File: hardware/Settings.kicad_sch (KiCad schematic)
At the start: 10 parts

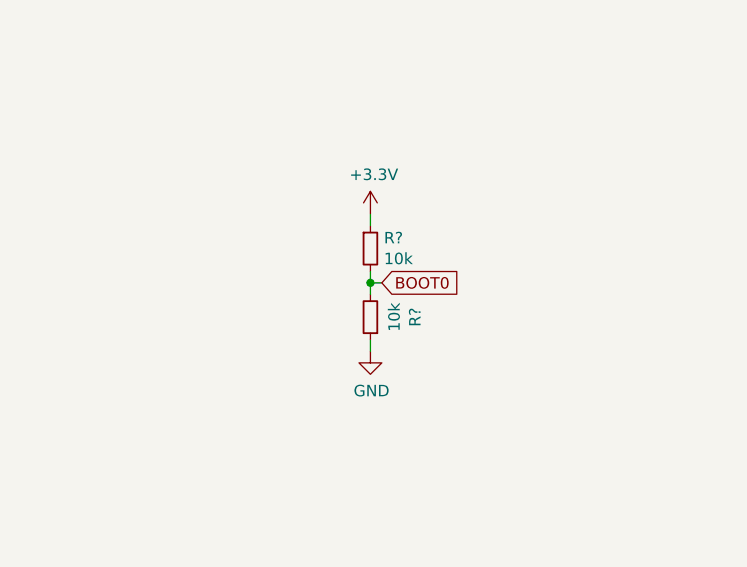
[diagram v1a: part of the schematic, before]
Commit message: added additional USB port and overall board update
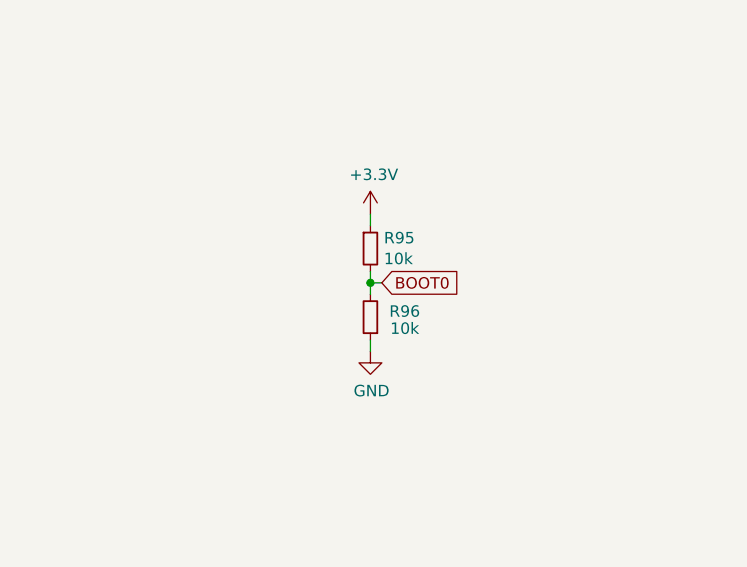
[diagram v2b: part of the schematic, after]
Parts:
- gave numbers to parts that had none: 2
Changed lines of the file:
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@@
   (symbol (lib_id "power:GND") (at 116.84 114.3 0) (unit 1)
     (in_bom yes) (on_board yes)
-    (property "Reference" "#PWR?" (id 0) (at 116.84 120.65 0)
+    (property "Reference" "#PWR0151" (id 0) (at 116.84 120.65 0)
       (effects (font (size 1.27 1.27)) hide)
     )
@@
   (symbol (lib_id "power:+3.3V") (at 227.965 85.09 0) (unit 1)
     (in_bom yes) (on_board yes)
-    (property "Reference" "#PWR?" (id 0) (at 227.965 88.9 0)
+    (property "Reference" "#PWR0153" (id 0) (at 227.965 88.9 0)
       (effects (font (size 1.27 1.27)) hide)
     )
@@
   (symbol (lib_id "power:GND") (at 93.345 114.3 0) (unit 1)
     (in_bom yes) (on_board yes)
-    (property "Reference" "#PWR?" (id 0) (at 93.345 120.65 0)
+    (property "Reference" "#PWR0149" (id 0) (at 93.345 120.65 0)
       (effects (font (size 1.27 1.27)) hide)
     )
@@
   (symbol (lib_id "Device:R_Small") (at 227.965 88.9 0) (unit 1)
     (in_bom yes) (on_board yes)
-    (property "Reference" "R?" (id 0) (at 229.4636 87.7316 0)
+    (property "Reference" "R95" (id 0) (at 229.4636 87.7316 0)
       (effects (font (size 1.27 1.27)) (justify left))
     )
@@
   (symbol (lib_id "power:GND") (at 74.93 114.3 0) (unit 1)
     (in_bom yes) (on_board yes)
-    (property "Reference" "#PWR?" (id 0) (at 74.93 120.65 0)
+    (property "Reference" "#PWR0150" (id 0) (at 74.93 120.65 0)
       (effects (font (size 1.27 1.27)) hide)
     )
@@
   (symbol (lib_id "power:GND") (at 227.965 100.33 0) (unit 1)
     (in_bom yes) (on_board yes)
-    (property "Reference" "#PWR?" (id 0) (at 227.965 106.68 0)
+    (property "Reference" "#PWR0152" (id 0) (at 227.965 106.68 0)
       (effects (font (size 1.27 1.27)) hide)
     )
@@
   (symbol (lib_id "Device:R_Small") (at 227.965 96.52 180) (unit 1)
     (in_bom yes) (on_board yes)
-    (property "Reference" "R?" (id 0) (at 232.9434 96.52 90))
-    (property "Value" "10k" (id 1) (at 230.632 96.52 90))
+    (property "Reference" "R96" (id 0) (at 231.775 95.885 0))
+    (property "Value" "10k" (id 1) (at 231.775 97.79 0))
     (property "Footprint" "Resistor_SMD:R_0603_1608Metric" (id 2) (at 227.965 96.52 0)
       (effects (font (size 1.27 1.27)) hide)
@@
   (symbol (lib_id "power:+3.3V") (at 93.345 99.06 0) (unit 1)
     (in_bom yes) (on_board yes)
-    (property "Reference" "#PWR?" (id 0) (at 93.345 102.87 0)
+    (property "Reference" "#PWR0147" (id 0) (at 93.345 102.87 0)
       (effects (font (size 1.27 1.27)) hide)
     )
@@
   (symbol (lib_id "power:+3.3V") (at 116.84 99.06 0) (unit 1)
     (in_bom yes) (on_board yes)
-    (property "Reference" "#PWR?" (id 0) (at 116.84 102.87 0)
+    (property "Reference" "#PWR0146" (id 0) (at 116.84 102.87 0)
       (effects (font (size 1.27 1.27)) hide)
     )
@@
   (symbol (lib_id "power:+3.3V") (at 74.93 99.06 0) (unit 1)
     (in_bom yes) (on_board yes)
-    (property "Reference" "#PWR?" (id 0) (at 74.93 102.87 0)
-      (effects (font (size 1.27 1.27)) hide)
-    )
+    (property "Reference" "#PWR0148" (id 0) (at 74.93 102.87 0)
+      (effects (font (size 1.27 1.27)) hide)
+    )

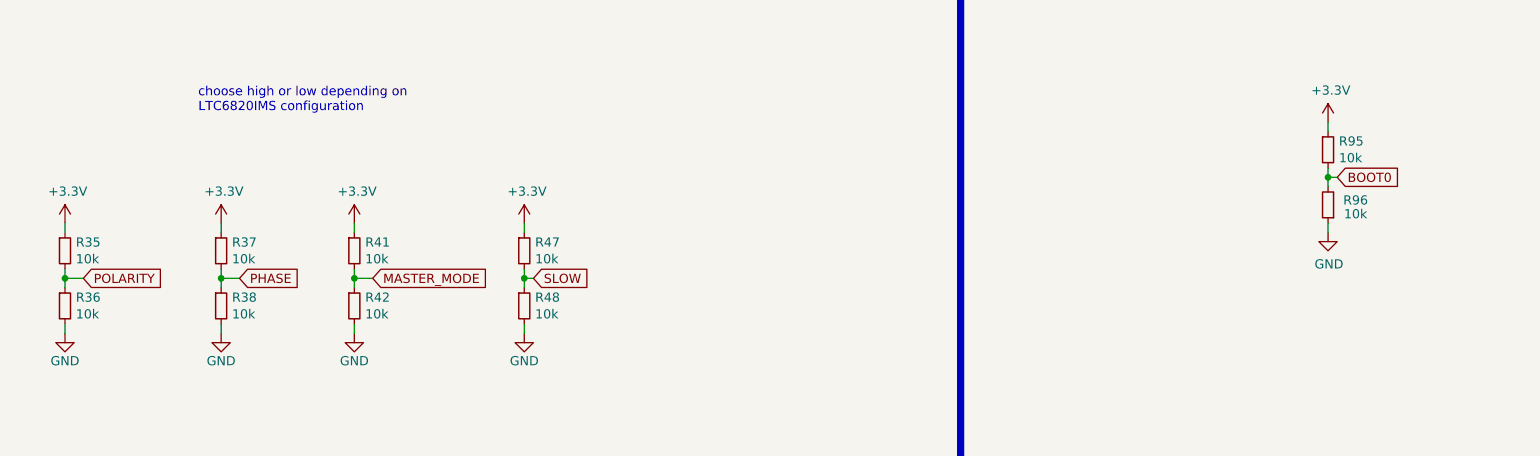
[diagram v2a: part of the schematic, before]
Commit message: Schematic readability update
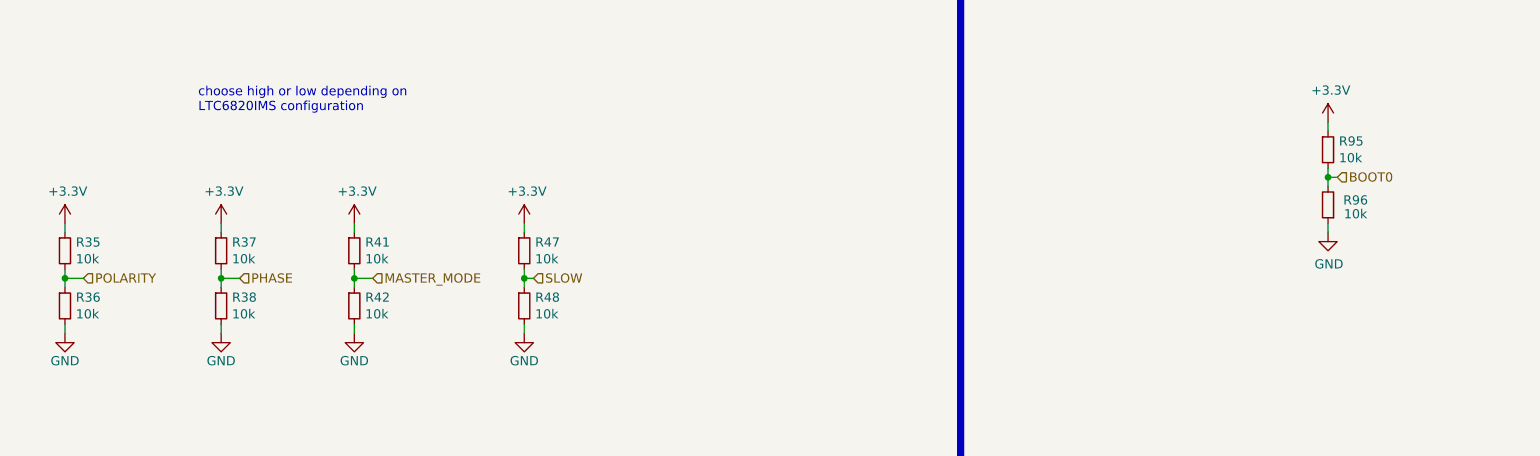
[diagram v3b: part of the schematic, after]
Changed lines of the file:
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@@
     (effects (font (size 5 5) (thickness 1) bold) (justify left bottom))
   )
-  (global_label "BOOT0" (shape input) (at 229.235 92.71 0) (fields_autoplaced)
+  (hierarchical_label "BOOT0" (shape input) (at 229.235 92.71 0)
     (effects (font (size 1.27 1.27)) (justify left))
-    (property "Intersheet References" "${INTERSHEET_REFS}" (id 0) (at 237.6673 92.7894 0)
-      (effects (font (size 1.27 1.27)) (justify left) hide)
-    )
   )
-  (global_label "POLARITY" (shape input) (at 55.88 106.68 0) (fields_autoplaced)
+  (hierarchical_label "POLARITY" (shape input) (at 55.88 106.68 0)
     (effects (font (size 1.27 1.27)) (justify left))
-    (property "Intersheet References" "${INTERSHEET_REFS}" (id 0) (at 66.8523 106.7594 0)
-      (effects (font (size 1.27 1.27)) (justify left) hide)
-    )
   )
-  (global_label "PHASE" (shape input) (at 77.47 106.68 0) (fields_autoplaced)
+  (hierarchical_label "SLOW" (shape input) (at 118.11 106.68 0)
     (effects (font (size 1.27 1.27)) (justify left))
-    (property "Intersheet References" "${INTERSHEET_REFS}" (id 0) (at 85.8418 106.6006 0)
-      (effects (font (size 1.27 1.27)) (justify left) hide)
-    )
   )
-  (global_label "SLOW" (shape input) (at 118.11 106.68 0) (fields_autoplaced)
+  (hierarchical_label "PHASE" (shape input) (at 77.47 106.68 0)
     (effects (font (size 1.27 1.27)) (justify left))
-    (property "Intersheet References" "${INTERSHEET_REFS}" (id 0) (at 125.4537 106.6006 0)
-      (effects (font (size 1.27 1.27)) (justify left) hide)
-    )
   )
-  (global_label "MASTER_MODE" (shape input) (at 95.885 106.68 0) (fields_autoplaced)
+  (hierarchical_label "MASTER_MODE" (shape input) (at 95.885 106.68 0)
     (effects (font (size 1.27 1.27)) (justify left))
-    (property "Intersheet References" "${INTERSHEET_REFS}" (id 0) (at 111.514 106.6006 0)
-      (effects (font (size 1.27 1.27)) (justify left) hide)
-    )
   )
   (symbol (lib_id "Device:R_Small") (at 74.93 102.87 0) (unit 1)

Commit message: remake in progress
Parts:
- removed R35, R36, R37, R38, R41, R42, R47, R48, R95, R96: 10k, Resistor_SMD:R_0603_1608Metric, symbol Device:R_Small
- added JP1: Polarity, Jumper:SolderJumper-3_P2.0mm_Open_TrianglePad1.0x1.5mm_NumberLabels, symbol Jumper:SolderJumper_3_Open
- added JP2, JP3: Phase, Jumper:SolderJumper-3_P2.0mm_Open_TrianglePad1.0x1.5mm_NumberLabels, symbol Jumper:SolderJumper_3_Open
- added JP4, JP5: Slow, Jumper:SolderJumper-3_P2.0mm_Open_TrianglePad1.0x1.5mm_NumberLabels, symbol Jumper:SolderJumper_3_Open
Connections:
- net +3V3: now also JP1.3 (B), JP2.3 (B), JP3.3 (B), JP4.3 (B), JP5.3 (B)
- net BOOT0: now also JP5.2 (C)
- net GND: now also JP1.1 (A), JP2.1 (A), JP3.1 (A), JP4.1 (A), JP5.1 (A)
- net MASTER_MODE: now also JP3.2 (C)
- net PHASE: now also JP2.2 (C)
- net POLARITY: now also JP1.2 (C)
- net SLOW: now also JP4.2 (C)

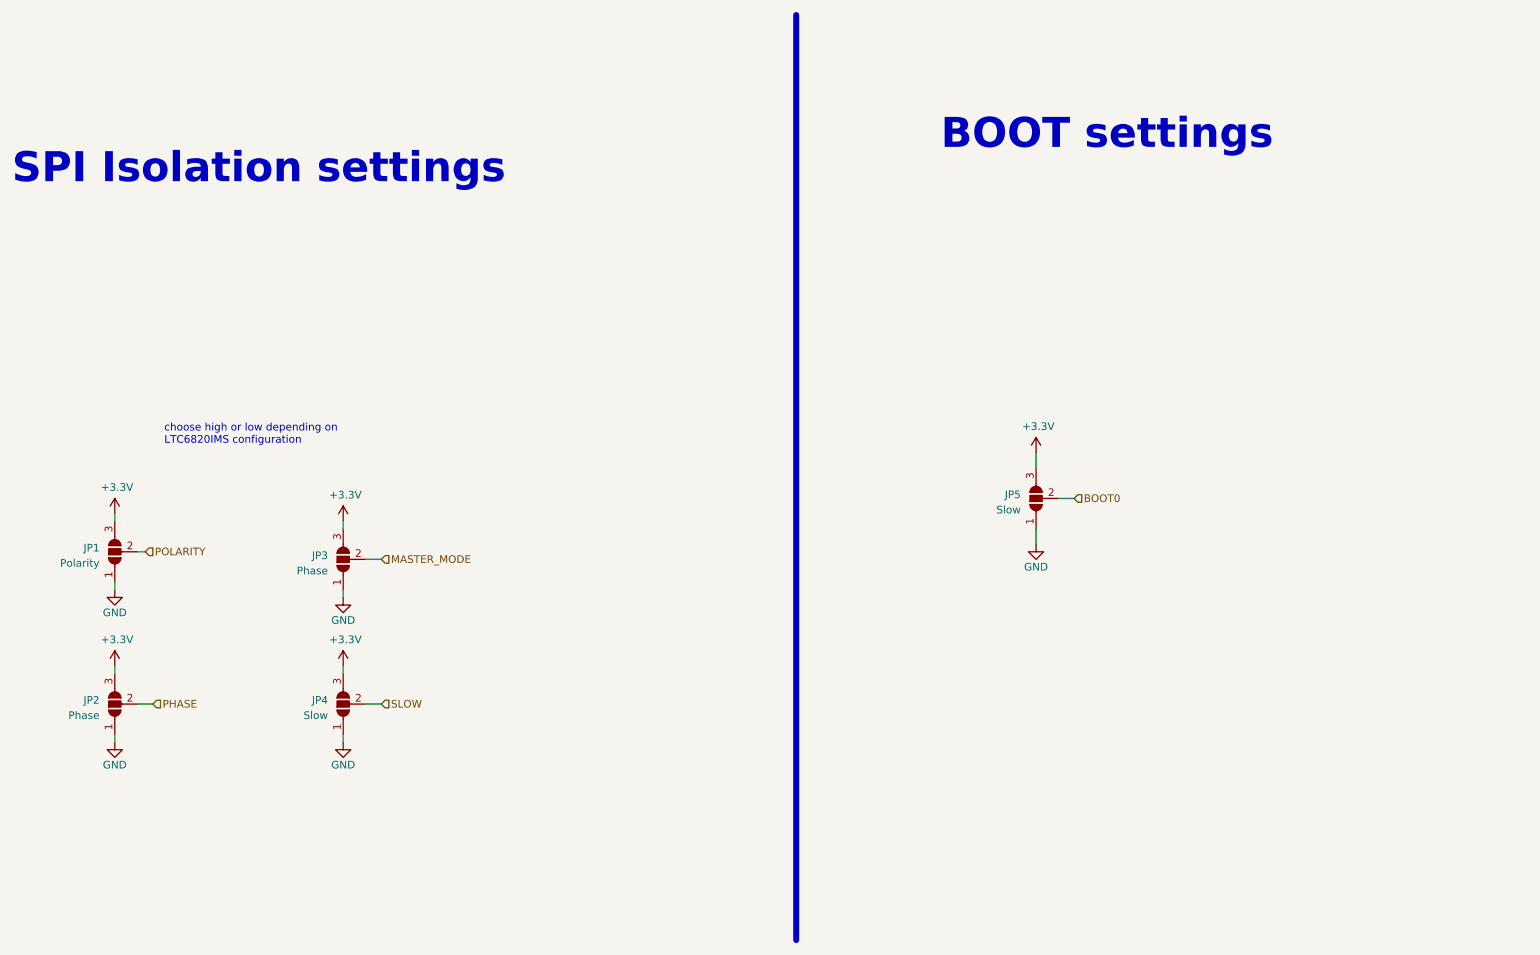
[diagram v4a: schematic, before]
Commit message: major changes: conn, fans, inputs and others
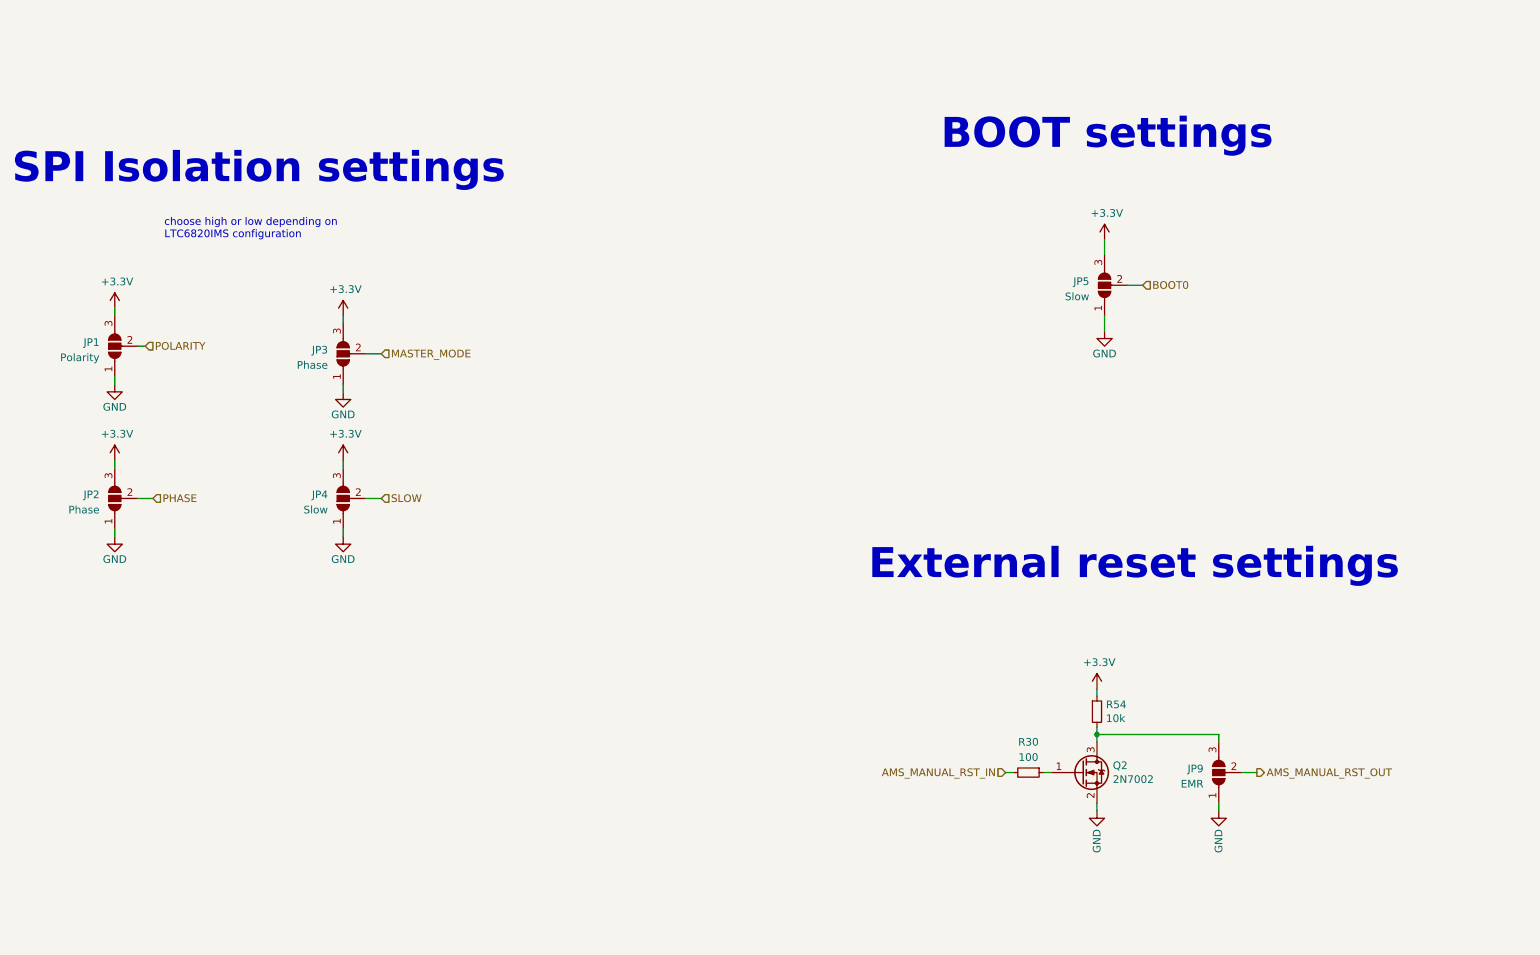
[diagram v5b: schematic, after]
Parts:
- added JP9: EMR, Jumper:SolderJumper-3_P2.0mm_Open_TrianglePad1.0x1.5mm_NumberLabels, symbol Jumper:SolderJumper_3_Open
- added Q2: 2N7002, Package_TO_SOT_SMD:SOT-23, symbol Transistor_FET:2N7002
- added R30: 100, Resistor_SMD:R_0603_1608Metric, symbol Device:R_Small
- added R54: 10k, Resistor_SMD:R_0603_1608Metric, symbol Device:R_Small
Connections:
- net +3V3: now also R54.1
- net GND: now also JP9.1 (A), Q2.2 (S)
- new net: Q2.1 (G), R30.1
- new net: JP9.3 (B), Q2.3 (D), R54.2
- new net AMS_MANUAL_RST_IN: R30.2
- new net AMS_MANUAL_RST_OUT: JP9.2 (C)
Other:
- note added: "External reset settings"
- moved on the sheet: JP1, JP2, JP3, JP4, JP5

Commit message: done
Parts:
- removed JP5: Slow, Jumper:SolderJumper-3_P2.0mm_Open_TrianglePad1.0x1.5mm_NumberLabels, symbol Jumper:SolderJumper_3_Open
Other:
- note removed: "BOOT settings"
- moved on the sheet: JP9, Q2, R30, R54

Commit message: WęGoRz AfTeR rEvIeW cOmMiT
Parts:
- removed JP9: EMR, Jumper:SolderJumper-3_P2.0mm_Open_TrianglePad1.0x1.5mm_NumberLabels, symbol Jumper:SolderJumper_3_Open
- removed Q2: 2N7002, Package_TO_SOT_SMD:SOT-23, symbol Transistor_FET:2N7002
- removed R30: 100, Resistor_SMD:R_0603_1608Metric, symbol Device:R_Small
- removed R54: 10k, Resistor_SMD:R_0603_1608Metric, symbol Device:R_Small
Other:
- note removed: "External reset settings"
